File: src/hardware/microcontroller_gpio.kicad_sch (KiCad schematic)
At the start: 12 parts

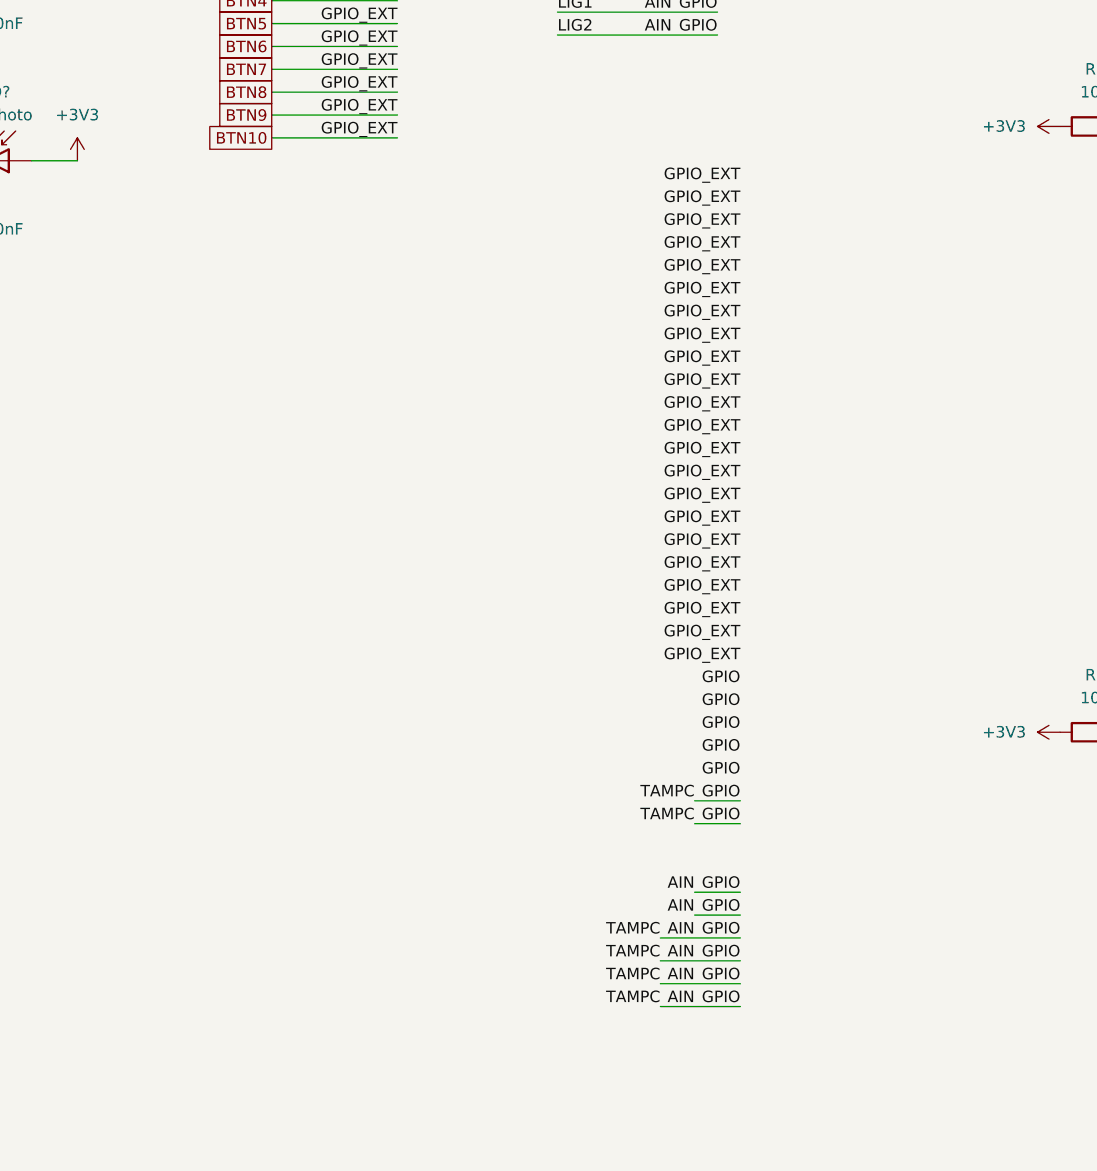
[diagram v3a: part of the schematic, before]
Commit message: Added display
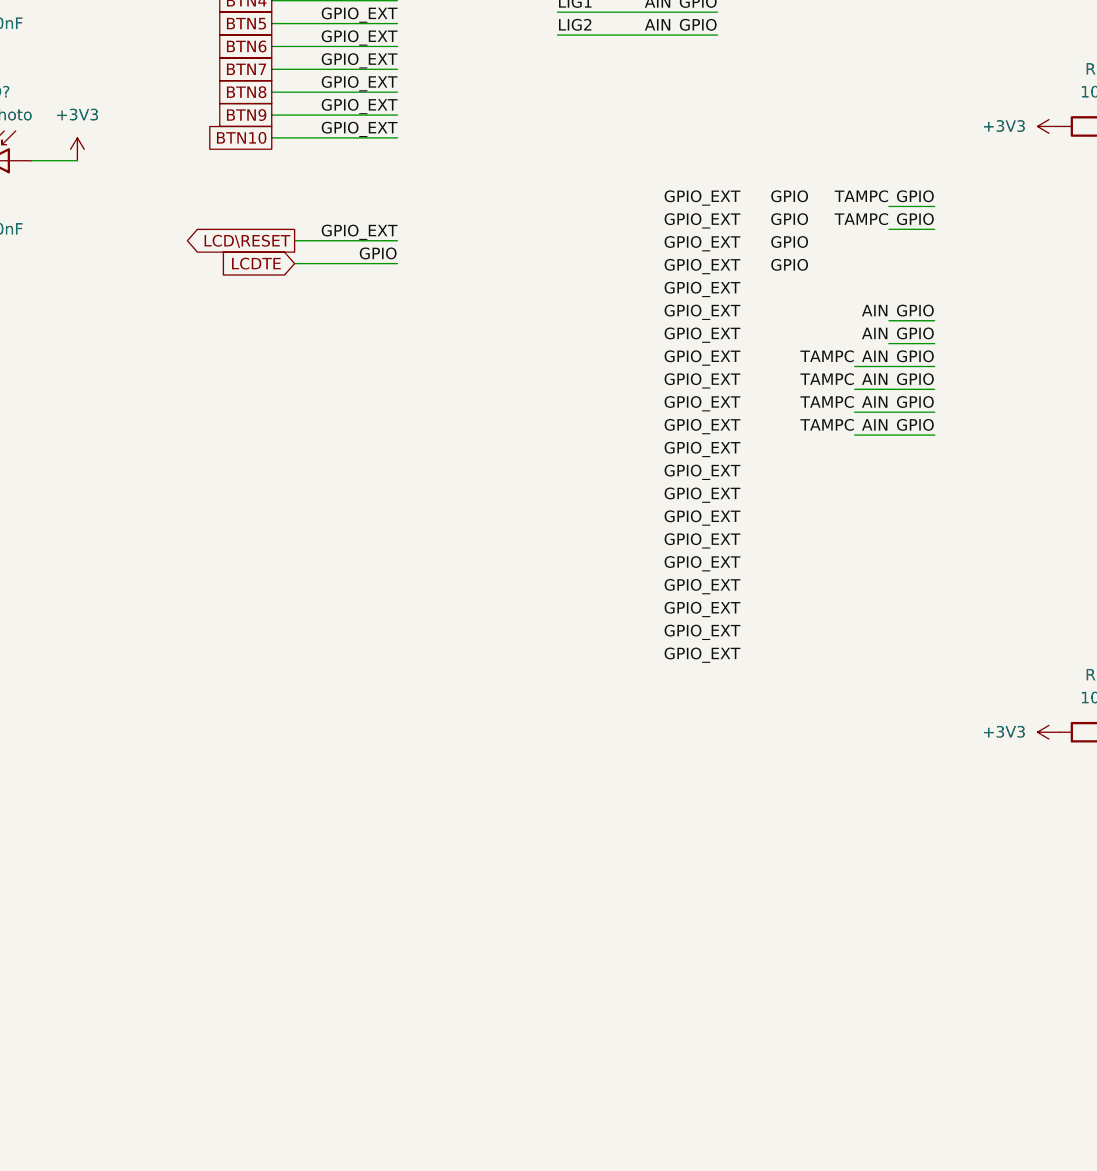
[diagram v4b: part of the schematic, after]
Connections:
- net AIN renamed LCDTE
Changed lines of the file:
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@@
 	(wire
 		(pts
-			(xy 165.1 143.51) (xy 156.21 143.51)
+			(xy 186.69 80.01) (xy 177.8 80.01)
 		)
 		(stroke
@@
 	(wire
 		(pts
-			(xy 165.1 135.89) (xy 160.02 135.89)
-		)
-		(stroke
-			(width 0)
-			(type default)
-		)
-	)
-	(wire
-		(pts
-			(xy 165.1 148.59) (xy 156.21 148.59)
+			(xy 186.69 72.39) (xy 181.61 72.39)
+		)
+		(stroke
+			(width 0)
+			(type default)
+		)
+	)
+	(wire
+		(pts
+			(xy 186.69 85.09) (xy 177.8 85.09)
 		)
 		(stroke
@@
 	(wire
 		(pts
-			(xy 165.1 146.05) (xy 156.21 146.05)
+			(xy 186.69 82.55) (xy 177.8 82.55)
 		)
 		(stroke
@@
 	(wire
 		(pts
-			(xy 165.1 138.43) (xy 160.02 138.43)
+			(xy 186.69 74.93) (xy 181.61 74.93)
 		)
 		(stroke
@@
 	(wire
 		(pts
-			(xy 165.1 140.97) (xy 156.21 140.97)
+			(xy 186.69 77.47) (xy 177.8 77.47)
 		)
 		(stroke
@@
 	(wire
 		(pts
-			(xy 165.1 125.73) (xy 160.02 125.73)
+			(xy 186.69 59.69) (xy 181.61 59.69)
 		)
 		(stroke
@@
 	(wire
 		(pts
+			(xy 115.57 66.04) (xy 127 66.04)
+		)
+		(stroke
+			(width 0)
+			(type default)
+		)
+	)
+	(wire
+		(pts
 			(xy 76.2 54.61) (xy 76.2 57.15)
 		)
@@
 	(wire
 		(pts
+			(xy 115.57 63.5) (xy 127 63.5)
+		)
+		(stroke
+			(width 0)
+			(type default)
+		)
+	)
+	(wire
+		(pts
 			(xy 209.55 60.96) (xy 220.98 60.96)
 		)
@@
 	(wire
 		(pts
-			(xy 165.1 128.27) (xy 160.02 128.27)
+			(xy 186.69 62.23) (xy 181.61 62.23)
 		)
 		(stroke
@@
 	)
 	(label "GPIO"
-		(at 165.1 148.59 180)
+		(at 186.69 85.09 180)
 		(effects
 			(font
@@
 	)
 	(label "GPIO"
-		(at 165.1 135.89 180)
+		(at 186.69 72.39 180)
 		(effects
 			(font
@@
 	)
 	(label "TAMPC"
-		(at 160.02 128.27 180)
+		(at 181.61 62.23 180)
 		(effects
 			(font
@@
 	)
 	(label "GPIO"
-		(at 165.1 143.51 180)
+		(at 186.69 80.01 180)
 		(effects
 			(font
@@
 	)
 	(label "TAMPC"
-		(at 156.21 146.05 180)
+		(at 177.8 82.55 180)
 		(effects
 			(font
@@
 	)
 	(label "GPIO"
-		(at 165.1 120.65 180)
+		(at 172.72 67.31 180)
 		(effects
 			(font
@@
 	)
 	(label "GPIO_EXT"
-		(at 165.1 57.15 180)
+		(at 127 63.5 180)
 		(effects
 			(font
@@
 	)
 	(label "AIN"
-		(at 160.02 148.59 180)
+		(at 181.61 85.09 180)
 		(effects
 			(font
@@
 	)
 	(label "GPIO"
-		(at 165.1 146.05 180)
+		(at 186.69 82.55 180)
 		(effects
 			(font
@@
 	)
 	(label "AIN"
-		(at 160.02 143.51 180)
+		(at 181.61 80.01 180)
 		(effects
 			(font
@@
 	)
 	(label "TAMPC"
-		(at 156.21 140.97 180)
+		(at 177.8 77.47 180)
 		(effects
 			(font
@@
 	)
 	(label "GPIO"
-		(at 165.1 128.27 180)
+		(at 186.69 62.23 180)
 		(effects
 			(font
@@
 	)
 	(label "GPIO"
-		(at 165.1 138.43 180)
+		(at 186.69 74.93 180)
 		(effects
 			(font
@@
 	)
 	(label "GPIO"
-		(at 165.1 113.03 180)
+		(at 172.72 59.69 180)
 		(effects
 			(font
@@
 	)
 	(label "GPIO"
-		(at 165.1 140.97 180)
+		(at 186.69 77.47 180)
 		(effects
 			(font
@@
 	)
 	(label "TAMPC"
-		(at 156.21 143.51 180)
+		(at 177.8 80.01 180)
 		(effects
 			(font
@@
 	)
 	(label "AIN"
-		(at 160.02 135.89 180)
+		(at 181.61 72.39 180)
 		(effects
 			(font
@@
 	)
 	(label "TAMPC"
-		(at 160.02 125.73 180)
+		(at 181.61 59.69 180)
 		(effects
 			(font
@@
 	)
 	(label "GPIO"
-		(at 165.1 125.73 180)
+		(at 186.69 59.69 180)
 		(effects
 			(font
@@
 	)
 	(label "TAMPC"
-		(at 156.21 148.59 180)
+		(at 177.8 85.09 180)
 		(effects
 			(font
@@
 	)
 	(label "AIN"
-		(at 160.02 146.05 180)
+		(at 181.61 82.55 180)
 		(effects
 			(font
@@
 	)
 	(label "AIN"
-		(at 160.02 138.43 180)
+		(at 181.61 74.93 180)
 		(effects
 			(font
@@
 	)
 	(label "GPIO"
-		(at 165.1 115.57 180)
+		(at 172.72 62.23 180)
 		(effects
 			(font
@@
 	)
 	(label "GPIO"
-		(at 165.1 123.19 180)
+		(at 127 66.04 180)
 		(effects
 			(font
@@
 	)
 	(label "GPIO"
-		(at 165.1 118.11 180)
+		(at 172.72 64.77 180)
 		(effects
 			(font
@@
 	)
 	(label "AIN"
-		(at 160.02 140.97 180)
+		(at 181.61 77.47 180)
 		(effects
 			(font
@@
 		)
 	)
+	(global_label "LCD\\RESET"
+		(shape output)
+		(at 115.57 63.5 180)
+		(fields_autoplaced yes)
+		(effects
+			(font
+				(size 1.27 1.27)
+			)
+			(justify right)
+		)
+		(property "Intersheetrefs" "${INTERSHEET_REFS}"
+			(at 102.4249 63.5 0)
+			(effects
+				(font
+					(size 1.27 1.27)
+				)
+				(justify right)
+				(hide yes)
+			)
+		)
+	)
 	(global_label "BTN10"
 		(shape passive)
@@
 			(effects
 				(font
+					(size 1.27 1.27)
+				)
+				(justify right)
+				(hide yes)
+			)
+		)
+	)
+	(global_label "LCDTE"
+		(shape input)
+		(at 115.57 66.04 180)
+		(fields_autoplaced yes)
+		(effects
+			(font
+				(size 1.27 1.27)
+			)
+			(justify right)
+		)
+		(property "Intersheetrefs" "${INTERSHEET_REFS}"
+			(at 106.9001 66.04 0)
+			(effects
+				(font

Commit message: Renamed symboles, added 3D models
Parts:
- removed U? (x4): PCAL6416AHF_128, HWQFN24_PCAL_NXP, symbol 2026-10-21_14-05-48:PCAL6416AHF_128
- added U? (x4): PCAL6416AHF_128, HWQFN24_PCAL_NXP, symbol PCAL6416AHF_128:PCAL6416AHF_128
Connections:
- net +3V3: now also U?.18 (ADDR), U?.21 (VDDP), U?.21 (VDDP), U?.23 (VDD), U?.23 (VDD)
- net BTN1: now also U?.1 (P0_0), U?.1 (P0_0), U?.10 (P1_0), U?.10 (P1_0), U?.11 (P1_1), U?.11 (P1_1), U?.12 (P1_2), U?.12 (P1_2), U?.13 (P1_3), U?.13 (P1_3), U?.14 (P1_4), U?.14 (P1_4), U?.15 (P1_5), U?.15 (P1_5), U?.16 (P1_6), U?.16 (P1_6), U?.17 (P1_7), U?.17 (P1_7), U?.2 (P0_1), U?.2 (P0_1), U?.3 (P0_2), U?.3 (P0_2), U?.4 (P0_3), U?.4 (P0_3), U?.5 (P0_4), U?.5 (P0_4), U?.6 (P0_5), U?.6 (P0_5), U?.7 (P0_6), U?.7 (P0_6), U?.8 (P0_7), U?.8 (P0_7)
- net GND: now also U?.18 (ADDR), U?.25 (EPAD), U?.25 (EPAD), U?.9 (VSS), U?.9 (VSS)
- net LCDTE: now also U?.22 (INT), U?.22 (INT)
- net SCL: now also U?.19 (SCL), U?.19 (SCL)
- net SDA: now also U?.20 (SDA), U?.20 (SDA)
- net at R?.2: now also U?.24 (RESET) (x2)

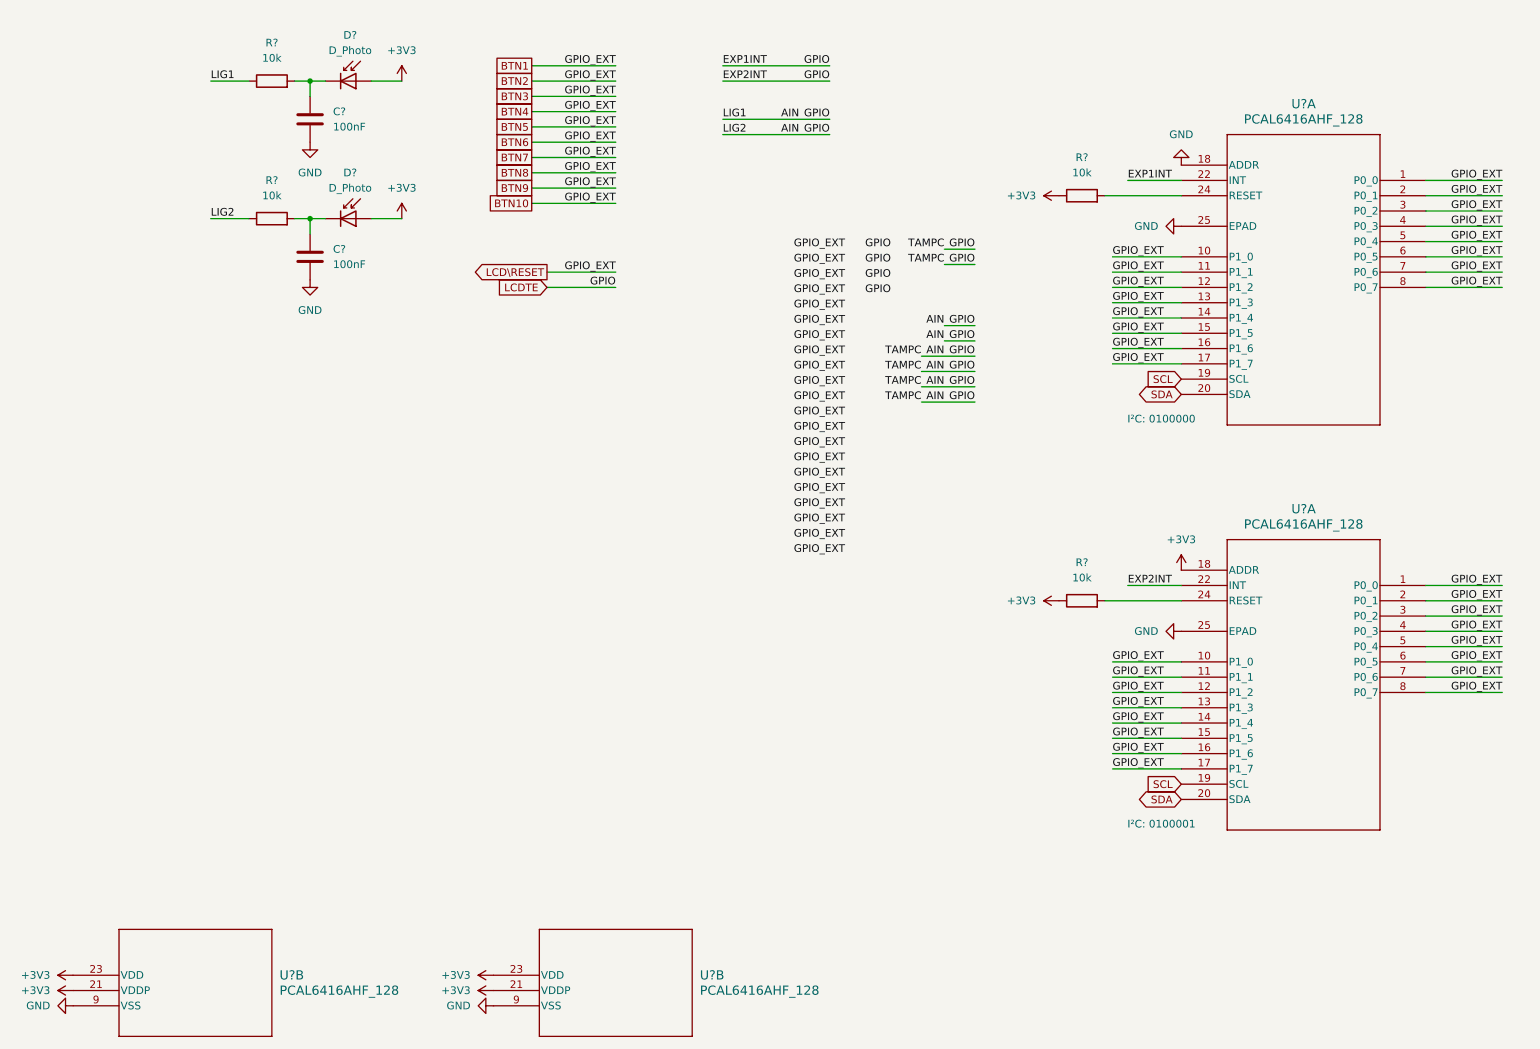
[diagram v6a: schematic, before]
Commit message: Replaced schematics, 3d models and footprints. Added vibration motor.
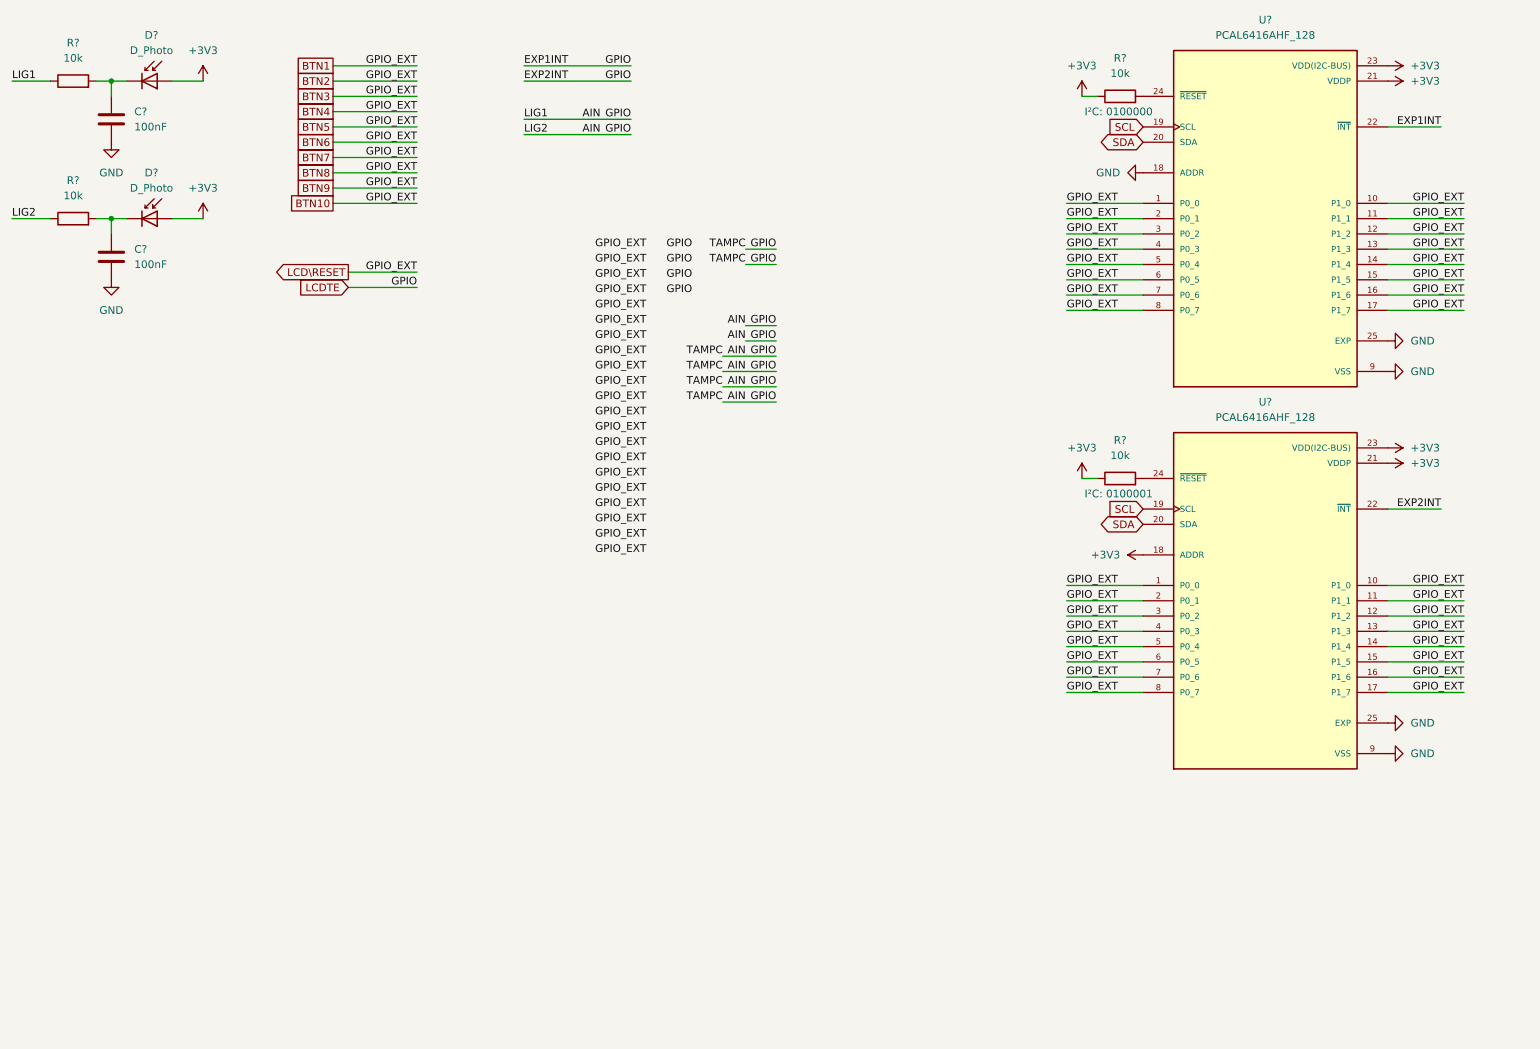
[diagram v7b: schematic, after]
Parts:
- removed R?: 10k, symbol Device:R
- removed U? (x4): PCAL6416AHF_128, HWQFN24_PCAL_NXP, symbol PCAL6416AHF_128:PCAL6416AHF_128
- added R?: 10k, symbol Device:R
- added U? (x2): PCAL6416AHF_128, PCAL6416AHF_128:QFN50P400X400X80-25N, symbol PCAL6416AHF_128:PCAL6416AHF_128
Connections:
- net +3V3: now also R?.1, U?.18 (ADDR), U?.21 (VDDP), U?.21 (VDDP), U?.23 (VDD(I2C-BUS)), U?.23 (VDD(I2C-BUS))
- net BTN1: now also U?.1 (P0_0), U?.1 (P0_0), U?.10 (P1_0), U?.10 (P1_0), U?.11 (P1_1), U?.11 (P1_1), U?.12 (P1_2), U?.12 (P1_2), U?.13 (P1_3), U?.13 (P1_3), U?.14 (P1_4), U?.14 (P1_4), U?.15 (P1_5), U?.15 (P1_5), U?.16 (P1_6), U?.16 (P1_6), U?.17 (P1_7), U?.17 (P1_7), U?.2 (P0_1), U?.2 (P0_1), U?.3 (P0_2), U?.3 (P0_2), U?.4 (P0_3), U?.4 (P0_3), U?.5 (P0_4), U?.5 (P0_4), U?.6 (P0_5), U?.6 (P0_5), U?.7 (P0_6), U?.7 (P0_6), U?.8 (P0_7), U?.8 (P0_7)
- net GND: now also U?.18 (ADDR), U?.25 (EXP), U?.25 (EXP), U?.9 (VSS), U?.9 (VSS)
- net LCDTE: now also U?.22 (~{INT}), U?.22 (~{INT})
- net SCL: now also U?.19 (SCL), U?.19 (SCL)
- net SDA: now also U?.20 (SDA), U?.20 (SDA)
- net at R?.2: now also U?.24 (~{RESET})
- new net: R?.2, U?.24 (~{RESET})
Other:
- moved on the sheet: C?, D?, R?

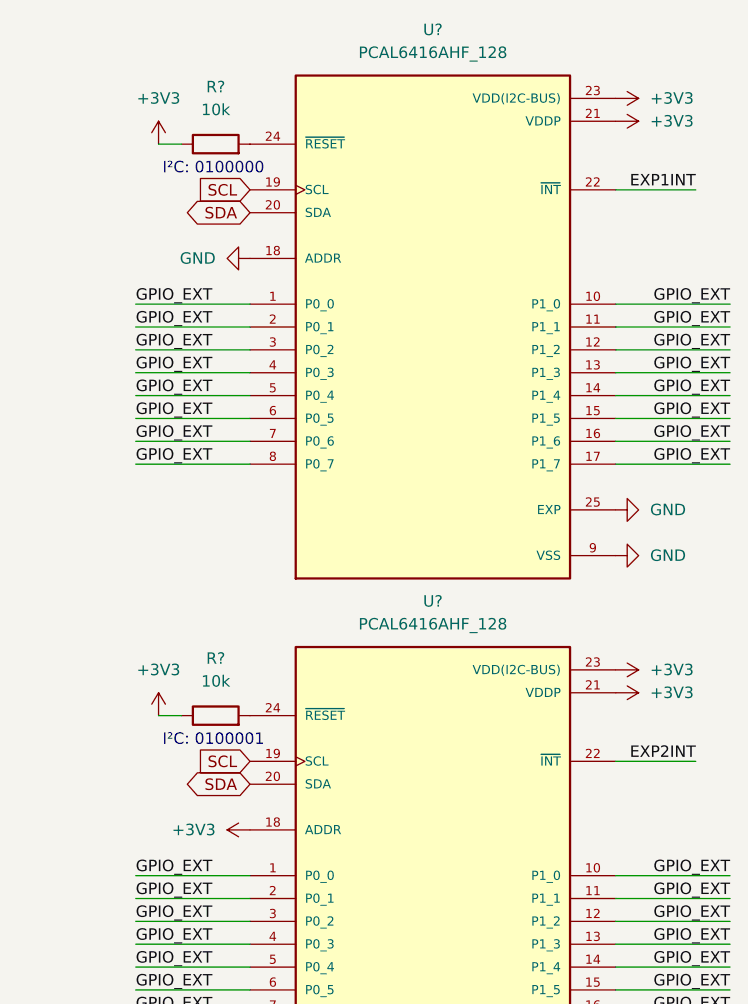
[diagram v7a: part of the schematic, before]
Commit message: Added LoRa
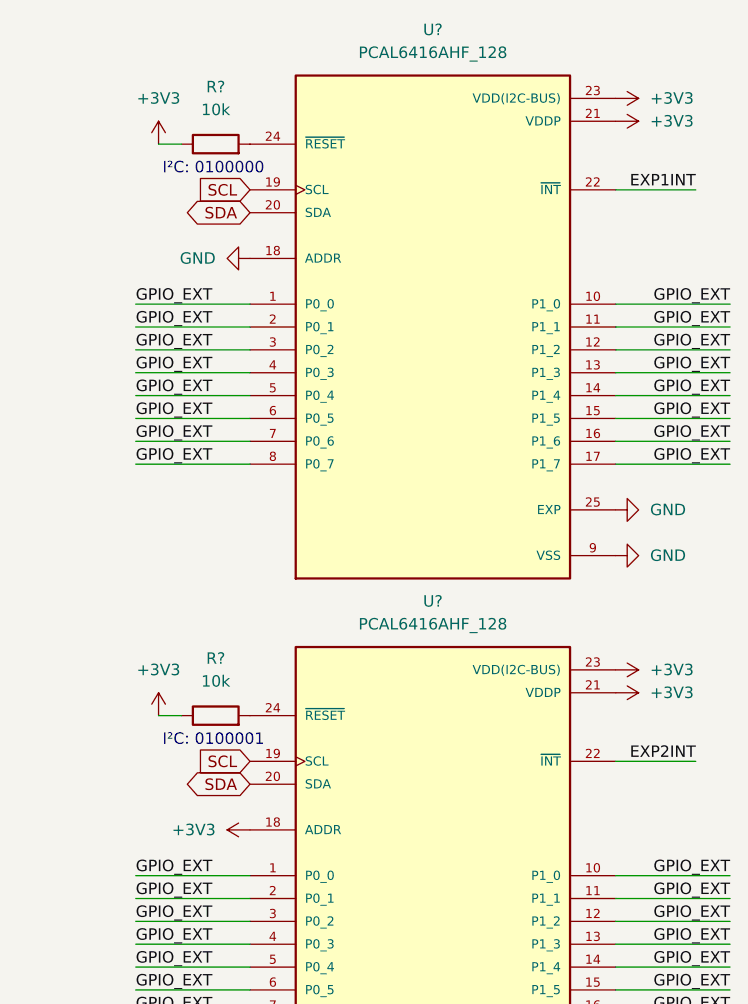
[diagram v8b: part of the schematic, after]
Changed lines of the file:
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@@
 		)
 		(property "Value" "+3V3"
-			(at 259.08 29.2101 90)
+			(at 259.08 29.2099 90)
 			(effects
 				(font
@@
 		(on_board yes)
 		(dnp no)
+		(fields_autoplaced yes)
 		(property "Reference" "#PWR0324"
 			(at 261.62 143.51 0)
@@
 		(on_board yes)
 		(dnp no)
+		(fields_autoplaced yes)
 		(property "Reference" "#PWR0323"
 			(at 261.62 138.43 0)
@@
 		)
 		(property "Value" "+3V3"
-			(at 259.08 92.7101 90)
+			(at 259.08 92.7099 90)
 			(effects
 				(font
@@
 		(on_board yes)
 		(dnp no)
+		(fields_autoplaced yes)
 		(property "Reference" "#PWR0320"
 			(at 218.44 110.49 0)
@@
 		)
 		(property "Value" "+3V3"
-			(at 210.82 110.4901 90)
+			(at 210.82 110.4899 90)
 			(effects
 				(font
@@
 		)
 		(property "Value" "+3V3"
-			(at 259.08 95.2501 90)
+			(at 259.08 95.2499 90)
 			(effects
 				(font
@@
 		)
 		(property "Value" "+3V3"
-			(at 259.08 31.7501 90)
+			(at 259.08 31.7499 90)
 			(effects
 				(font
@@
 		(on_board yes)
 		(dnp no)
+		(fields_autoplaced yes)
 		(property "Reference" "#PWR044"
 			(at 261.62 74.93 0)
@@
 		(on_board yes)
 		(dnp no)
+		(fields_autoplaced yes)
 		(property "Reference" "#PWR06"
 			(at 261.62 80.01 0)
